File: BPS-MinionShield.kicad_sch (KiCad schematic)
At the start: 91 parts, among them J1 TempConn1, J2 TempConn2, J3 Conn_01x24_Female, T1 TestPoint, T10 TestPoint, T11 TestPoint, T12 TestPoint, T13 TestPoint, T14 TestPoint, T15 TestPoint, T16 TestPoint, T2 TestPoint, T3 TestPoint, T4 TestPoint, T5 TestPoint, T6 TestPoint, T7 TestPoint, T8 TestPoint, T9 TestPoint

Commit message: generated BOM
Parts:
- added GND1, GND2: TestPoint, TestPoint:TestPoint_THTPad_D1.5mm_Drill0.7mm, symbol Connector:TestPoint
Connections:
- net GND: now also GND1.1, GND2.1
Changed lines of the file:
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@@
   (junction (at 196.215 150.495) (diameter 0) (color 0 0 0 0)
   )
+  (junction (at 48.26 167.64) (diameter 0) (color 0 0 0 0)
+  )
   (junction (at 88.9 31.75) (diameter 0) (color 0 0 0 0)
   )
@@
   (junction (at 120.65 109.22) (diameter 0) (color 0 0 0 0)
   )
+  (junction (at 48.26 173.99) (diameter 0) (color 0 0 0 0)
+  )
   (junction (at 132.715 150.495) (diameter 0) (color 0 0 0 0)
   )
@@
     (stroke (width 0) (type default) (color 0 0 0 0))
   )
+  (wire (pts (xy 48.26 173.99) (xy 48.26 167.64))
+    (stroke (width 0) (type default) (color 0 0 0 0))
+  )
   (wire (pts (xy 196.215 136.525) (xy 196.215 139.065))
     (stroke (width 0) (type default) (color 0 0 0 0))
@@
     (stroke (width 0) (type default) (color 0 0 0 0))
   )
+  (wire (pts (xy 48.26 167.64) (xy 48.26 161.925))
+    (stroke (width 0) (type default) (color 0 0 0 0))
+  )
   (wire (pts (xy 48.26 161.925) (xy 45.72 161.925))
     (stroke (width 0) (type default) (color 0 0 0 0))
@@
     (stroke (width 0) (type default) (color 0 0 0 0))
   )
-  (wire (pts (xy 48.26 164.465) (xy 48.26 161.925))
+  (wire (pts (xy 48.26 178.435) (xy 48.26 173.99))
     (stroke (width 0) (type default) (color 0 0 0 0))
   )
@@
     (pin "1")
   )
-  (symbol (lib_id "power:GND") (at 48.26 164.465 0) (unit 1)
+  (symbol (lib_id "power:GND") (at 48.26 178.435 0) (unit 1)
     (in_bom yes) (on_board yes)
-    (property "Reference" "#PWR06" (id 0) (at 48.26 170.815 0)
+    (property "Reference" "#PWR06" (id 0) (at 48.26 184.785 0)
       (effects (font (size 1.27 1.27)) hide)
     )
-    (property "Value" "GND" (id 1) (at 48.387 168.8592 0))
-    (property "Footprint" "" (id 2) (at 48.26 164.465 0)
+    (property "Value" "GND" (id 1) (at 48.387 182.8292 0))
+    (property "Footprint" "" (id 2) (at 48.26 178.435 0)
       (effects (font (size 1.27 1.27)) hide)
     )
-    (property "Datasheet" "" (id 3) (at 48.26 164.465 0)
+    (property "Datasheet" "" (id 3) (at 48.26 178.435 0)
       (effects (font (size 1.27 1.27)) hide)
     )
@@
     (pin "1")
   )
+  (symbol (lib_id "Connector:TestPoint") (at 48.26 173.99 270) (unit 1)
+    (in_bom yes) (on_board yes) (fields_autoplaced)
+    (property "Reference" "GND2" (id 0) (at 53.34 172.7199 90)
+      (effects (font (size 1.27 1.27)) (justify left))
+    )
+    (property "Value" "TestPoint" (id 1) (at 53.34 175.2599 90)
+      (effects (font (size 1.27 1.27)) (justify left))
+    )
+    (property "Footprint" "TestPoint:TestPoint_THTPad_D1.5mm_Drill0.7mm" (id 2) (at 48.26 179.07 0)
+      (effects (font (size 1.27 1.27)) hide)
+    )
+    (property "Datasheet" "~" (id 3) (at 48.26 179.07 0)
+      (effects (font (size 1.27 1.27)) hide)
+    )
+    (pin "1")
+  )
   (symbol (lib_id "Device:R_US") (at 196.215 104.775 180) (unit 1)
     (in_bom yes) (on_board yes)
@@
     (pin "2")
   )
+  (symbol (lib_id "Connector:TestPoint") (at 48.26 167.64 270) (unit 1)
+    (in_bom yes) (on_board yes) (fields_autoplaced)
+    (property "Reference" "GND1" (id 0) (at 53.34 166.3699 90)
+      (effects (font (size 1.27 1.27)) (justify left))
+    )
+    (property "Value" "TestPoint" (id 1) (at 53.34 168.9099 90)
+      (effects (font (size 1.27 1.27)) (justify left))
+    )
+    (property "Footprint" "TestPoint:TestPoint_THTPad_D1.5mm_Drill0.7mm" (id 2) (at 48.26 172.72 0)
+      (effects (font (size 1.27 1.27)) hide)
+    )
+    (property "Datasheet" "~" (id 3) (at 48.26 172.72 0)
+      (effects (font (size 1.27 1.27)) hide)
+    )
+    (pin "1")
+  )
   (symbol (lib_id "Device:C_Small") (at 120.65 40.64 180) (unit 1)
     (in_bom yes) (on_board yes)
@@
       (reference "FB16") (unit 1) (value "2.2k") (footprint "Inductor_SMD:L_0805_2012Metric")
     )
+    (path "/90b9d833-67a5-4957-9778-5ee0e82ad02c"
+      (reference "GND1") (unit 1) (value "TestPoint") (footprint "TestPoint:TestPoint_THTPad_D1.5mm_Drill0.7mm")
+    )
+    (path "/5bceed01-0866-41e6-9701-c7a4fbbbfa24"
+      (reference "GND2") (unit 1) (value "TestPoint") (footprint "TestPoint:TestPoint_THTPad_D1.5mm_Drill0.7mm")
+    )
     (path "/00000000-0000-0000-0000-00005dc3a36f"

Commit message: made stuff pretty and rerouted
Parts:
- added FB17, FB18: 2.2k, Inductor_SMD:L_0805_2012Metric, symbol Device:FerriteBead_Small
- added GND3, GND4, GND5: TestPoint, TestPoint:TestPoint_THTPad_D1.5mm_Drill0.7mm, symbol Connector:TestPoint
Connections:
- net GND: now also FB17.1, FB18.1, GND3.1, GND4.1, GND5.1; no longer J3.1 (Pin_1), J3.13 (Pin_13), J3.14 (Pin_14), J3.2 (Pin_2)
- new net: FB17.2, J3.1 (Pin_1), J3.2 (Pin_2)
- new net: FB18.2, J3.13 (Pin_13), J3.14 (Pin_14)

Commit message: redid the vias
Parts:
- removed T1, T10, T11, T12, T13, T14, T15, T16, T2, T3, T4, T5, T6, T7, T8, T9: TestPoint, TestPoint:TestPoint_THTPad_D1.5mm_Drill0.7mm, symbol Connector:TestPoint

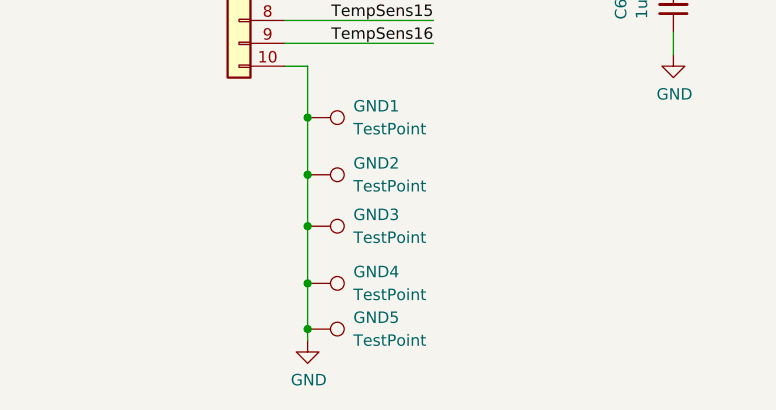
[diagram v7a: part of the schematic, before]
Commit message: removed some gnd test points
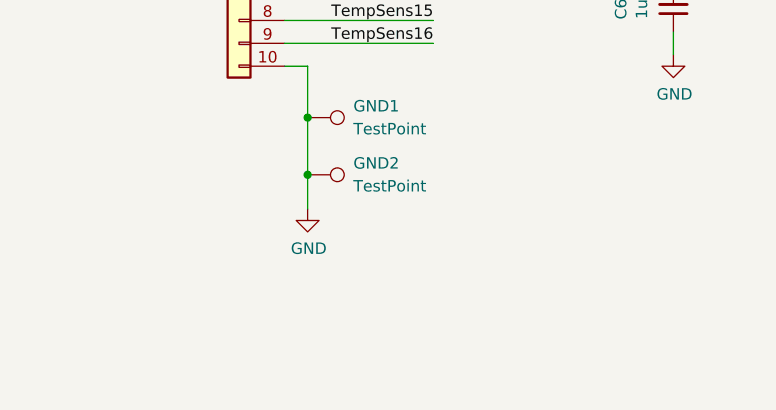
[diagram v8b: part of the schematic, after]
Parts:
- removed GND3, GND4, GND5: TestPoint, TestPoint:TestPoint_THTPad_D1.5mm_Drill0.7mm, symbol Connector:TestPoint
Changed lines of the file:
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@@
     (rev "2.2")
   )
-  (junction (at 48.26 179.705) (diameter 0) (color 0 0 0 0)
-  )
   (junction (at 88.9 112.395) (diameter 0) (color 0 0 0 0)
   )
@@
   (junction (at 164.465 112.395) (diameter 0) (color 0 0 0 0)
   )
-  (junction (at 48.26 186.055) (diameter 0) (color 0 0 0 0)
-  )
   (junction (at 132.715 35.56) (diameter 0) (color 0 0 0 0)
   )
   (junction (at 196.215 150.495) (diameter 0) (color 0 0 0 0)
   )
+  (junction (at 48.26 173.99) (diameter 0) (color 0 0 0 0)
+  )
   (junction (at 48.26 167.64) (diameter 0) (color 0 0 0 0)
   )
@@
   (junction (at 152.4 112.395) (diameter 0) (color 0 0 0 0)
   )
-  (junction (at 48.26 173.99) (diameter 0) (color 0 0 0 0)
-  )
   (junction (at 132.715 150.495) (diameter 0) (color 0 0 0 0)
   )
@@
   )
   (junction (at 100.965 112.395) (diameter 0) (color 0 0 0 0)
-  )
-  (junction (at 48.26 191.135) (diameter 0) (color 0 0 0 0)
   )
   (junction (at 152.4 35.56) (diameter 0) (color 0 0 0 0)
@@
     (stroke (width 0) (type default) (color 0 0 0 0))
   )
-  (wire (pts (xy 48.26 191.135) (xy 48.26 186.055))
-    (stroke (width 0) (type default) (color 0 0 0 0))
-  )
   (wire (pts (xy 196.215 136.525) (xy 196.215 139.065))
     (stroke (width 0) (type default) (color 0 0 0 0))
@@
     (stroke (width 0) (type default) (color 0 0 0 0))
   )
-  (wire (pts (xy 48.26 186.055) (xy 48.26 179.705))
-    (stroke (width 0) (type default) (color 0 0 0 0))
-  )
-  (wire (pts (xy 48.26 179.705) (xy 48.26 173.99))
-    (stroke (width 0) (type default) (color 0 0 0 0))
-  )
   (wire (pts (xy 120.65 99.695) (xy 120.65 112.395))
     (stroke (width 0) (type default) (color 0 0 0 0))
@@
     (stroke (width 0) (type default) (color 0 0 0 0))
   )
+  (wire (pts (xy 48.26 173.99) (xy 48.26 177.8))
+    (stroke (width 0) (type default) (color 0 0 0 0))
+  )
   (wire (pts (xy 123.19 35.56) (xy 120.65 35.56))
     (stroke (width 0) (type default) (color 0 0 0 0))
@@
   )
   (wire (pts (xy 196.215 108.585) (xy 196.215 112.395))
-    (stroke (width 0) (type default) (color 0 0 0 0))
-  )
-  (wire (pts (xy 48.26 192.405) (xy 48.26 191.135))
     (stroke (width 0) (type default) (color 0 0 0 0))
   )
@@
     (pin "1")
   )
-  (symbol (lib_id "power:GND") (at 48.26 192.405 0) (unit 1)
-    (in_bom yes) (on_board yes)
-    (property "Reference" "#PWR06" (id 0) (at 48.26 198.755 0)
-      (effects (font (size 1.27 1.27)) hide)
-    )
-    (property "Value" "GND" (id 1) (at 48.387 196.7992 0))
-    (property "Footprint" "" (id 2) (at 48.26 192.405 0)
-      (effects (font (size 1.27 1.27)) hide)
-    )
-    (property "Datasheet" "" (id 3) (at 48.26 192.405 0)
-      (effects (font (size 1.27 1.27)) hide)
-    )
-    (pin "1")
-  )
   (symbol (lib_id "power:GND") (at 33.02 136.525 0) (unit 1)
     (in_bom yes) (on_board yes)
@@
     )
     (property "Datasheet" "" (id 3) (at 196.215 136.525 0)
-      (effects (font (size 1.27 1.27)) hide)
-    )
-    (pin "1")
-  )
-  (symbol (lib_id "Connector:TestPoint") (at 48.26 191.135 270) (unit 1)
-    (in_bom yes) (on_board yes) (fields_autoplaced)
-    (property "Reference" "GND5" (id 0) (at 53.34 189.8649 90)
-      (effects (font (size 1.27 1.27)) (justify left))
-    )
-    (property "Value" "TestPoint" (id 1) (at 53.34 192.4049 90)
-      (effects (font (size 1.27 1.27)) (justify left))
-    )
-    (property "Footprint" "TestPoint:TestPoint_THTPad_D1.5mm_Drill0.7mm" (id 2) (at 48.26 196.215 0)
-      (effects (font (size 1.27 1.27)) hide)
-    )
-    (property "Datasheet" "~" (id 3) (at 48.26 196.215 0)
       (effects (font (size 1.27 1.27)) hide)
     )
@@
     (pin "2")
   )
+  (symbol (lib_id "power:GND") (at 48.26 177.8 0) (unit 1)
+    (in_bom yes) (on_board yes)
+    (property "Reference" "#PWR0101" (id 0) (at 48.26 184.15 0)
+      (effects (font (size 1.27 1.27)) hide)
+    )
+    (property "Value" "GND" (id 1) (at 48.387 182.1942 0))
+    (property "Footprint" "" (id 2) (at 48.26 177.8 0)
+      (effects (font (size 1.27 1.27)) hide)
+    )
+    (property "Datasheet" "" (id 3) (at 48.26 177.8 0)
+      (effects (font (size 1.27 1.27)) hide)
+    )
+    (pin "1")
+  )
   (symbol (lib_id "Device:C_Small") (at 152.4 40.64 180) (unit 1)
     (in_bom yes) (on_board yes)
@@
     (pin "2")
   )
-  (symbol (lib_id "Connector:TestPoint") (at 48.26 186.055 270) (unit 1)
-    (in_bom yes) (on_board yes) (fields_autoplaced)
-    (property "Reference" "GND4" (id 0) (at 53.34 184.7849 90)
-      (effects (font (size 1.27 1.27)) (justify left))
-    )
-    (property "Value" "TestPoint" (id 1) (at 53.34 187.3249 90)
-      (effects (font (size 1.27 1.27)) (justify left))
-    )
-    (property "Footprint" "TestPoint:TestPoint_THTPad_D1.5mm_Drill0.7mm" (id 2) (at 48.26 191.135 0)
-      (effects (font (size 1.27 1.27)) hide)
-    )
-    (property "Datasheet" "~" (id 3) (at 48.26 191.135 0)
-      (effects (font (size 1.27 1.27)) hide)
-    )
-    (pin "1")
-  )
   (symbol (lib_id "Device:FerriteBead_Small") (at 201.295 35.56 90) (unit 1)
     (in_bom yes) (on_board yes)
@@
     (pin "1")
   )
-  (symbol (lib_id "Connector:TestPoint") (at 48.26 179.705 270) (unit 1)
-    (in_bom yes) (on_board yes) (fields_autoplaced)
-    (property "Reference" "GND3" (id 0) (at 53.34 178.4349 90)
-      (effects (font (size 1.27 1.27)) (justify left))
-    )
-    (property "Value" "TestPoint" (id 1) (at 53.34 180.9749 90)
-      (effects (font (size 1.27 1.27)) (justify left))
-    )
-    (property "Footprint" "TestPoint:TestPoint_THTPad_D1.5mm_Drill0.7mm" (id 2) (at 48.26 184.785 0)
-      (effects (font (size 1.27 1.27)) hide)
-    )
-    (property "Datasheet" "~" (id 3) (at 48.26 184.785 0)
-      (effects (font (size 1.27 1.27)) hide)
-    )
-    (pin "1")
-  )
   (symbol (lib_id "Device:R_US") (at 95.25 35.56 90) (unit 1)
     (in_bom yes) (on_board yes)
@@
       (reference "#PWR05") (unit 1) (value "+5V") (footprint "")
     )
-    (path "/00000000-0000-0000-0000-00005db5ee87"
-      (reference "#PWR06") (unit 1) (value "GND") (footprint "")
-    )
     (path "/00000000-0000-0000-0000-00005dc8996b"
       (reference "#PWR07") (unit 1) (value "+5V") (footprint "")
@@
       (reference "#PWR042") (unit 1) (value "GND") (footprint "")
     )
+    (path "/751eacfa-8a42-4723-a47b-87fc97d190bc"
+      (reference "#PWR0101") (unit 1) (value "GND") (footprint "")
+    )
     (path "/00000000-0000-0000-0000-00005db6d140"
       (reference "C1") (unit 1) (value "100n") (footprint "Capacitor_SMD:C_0805_2012Metric")
@@
       (reference "GND2") (unit 1) (value "TestPoint") (footprint "TestPoint:TestPoint_THTPad_D1.5mm_Drill0.7mm")
     )
-    (path "/afbec3c9-7457-4eda-ae2e-e63cbd769db5"
-      (reference "GND3") (unit 1) (value "TestPoint") (footprint "TestPoint:TestPoint_THTPad_D1.5mm_Drill0.7mm")
-    )
-    (path "/9e9641ff-5180-4c82-bef4-39185230197e"
-      (reference "GND4") (unit 1) (value "TestPoint") (footprint "TestPoint:TestPoint_THTPad_D1.5mm_Drill0.7mm")
-    )
-    (path "/50839b99-654a-4b96-b475-82d5f7529035"
-      (reference "GND5") (unit 1) (value "TestPoint") (footprint "TestPoint:TestPoint_THTPad_D1.5mm_Drill0.7mm")
-    )
     (path "/00000000-0000-0000-0000-00005dc3a36f"
